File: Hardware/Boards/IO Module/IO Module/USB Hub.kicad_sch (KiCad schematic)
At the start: 0 parts

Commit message: Updated IO Module Schematics
Added Power, USB hub and USB-JTAG circuits
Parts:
- added C29: 10nF, Capacitor_SMD:C_0402_1005Metric, symbol Device:C_Small
- added C30, C32, C33, C34, C40, C41, C42, C43, C44, C45, C46, C47, C52, C53, C54, C55, C56, C57, C58, C59, C60, C61: 100nF, Capacitor_SMD:C_0402_1005Metric, symbol Device:C_Small
- added C31, C36, C48, C51: 1uF, Capacitor_SMD:C_0402_1005Metric, symbol Device:C_Small
- added C35, C37, C38, C39: 10uF, Capacitor_SMD:C_0603_1608Metric, symbol Device:C_Small
- added C49, C50: 18pF, Capacitor_SMD:C_0402_1005Metric, symbol Device:C_Small
- added D5: 1V1 FLT, LED_SMD:LED_0603_1608Metric, symbol Device:LED
- added Q2: IRLML6244, Package_TO_SOT_SMD:SOT-23, symbol Transistor_FET:IRLML6244
- added R32: 3.74K, Resistor_SMD:R_0402_1005Metric, symbol Device:R_US
- added R33, R38, R39, R40, R41: 10K, Resistor_SMD:R_0402_1005Metric, symbol Device:R_US
- added R34: 3.3K, Resistor_SMD:R_0402_1005Metric, symbol Device:R_US
- added R35: 1.13K, Resistor_SMD:R_0402_1005Metric, symbol Device:R_US
- added R36: 44.2K, Resistor_SMD:R_0402_1005Metric, symbol Device:R_US
- added R37: 1M, Resistor_SMD:R_0402_1005Metric, symbol Device:R_US
- added R42, R43, R45, R46, R47, R48, R49, R50, R51, R52: 33R, Resistor_SMD:R_0402_1005Metric, symbol Device:R_US
- added R44: 9.53K, Resistor_SMD:R_0402_1005Metric, symbol Device:R_US
- added U5: TUSB8041, Package_DFN_QFN:QFN-64-1EP_9x9mm_P0.5mm_EP6x6mm_ThermalVias, symbol Interface_USB:TUSB8041
- added U6: TPS74801AWDRC, Package_SON:VSON-10-1EP_3x3mm_P0.5mm_EP1.65x2.4mm_ThermalVias, symbol Regulator_Linear:TPS74801AWDRC
- added U7: TUSB542, IO_Module:TUSB542, symbol IO_Module:TUSB542
- added Y1: 24Mhz, Oscillator:Oscillator_SMD_Abracon_ASE-4Pin_3.2x2.5mm, symbol Device:Crystal_GND24_Small
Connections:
- new net: C48.1, U5.50 (GRSTz)
- new net: R44.1, U5.64 (USB_R1)
- new net: R40.1, R41.2, U7.10 (CFG_B2)
- new net: D5.1 (K), U6.3 (PG)
- new net: C29.1, U6.7 (SS)
- new net: D5.2 (A), R34.2
- new net: Q2.3 (D), R39.1, U7.16 (SEL)
- new net +1V1: C37.1, C38.1, C39.1, C40.1, C41.1, C42.1, C43.1, C44.1, C45.1, C46.1, C47.1, R32.2, U5.13 (VDD), U5.21 (VDD), U5.28 (VDD), U5.31 (VDD), U5.5 (VDD), U5.51 (VDD), U5.57 (VDD), U5.8 (VDD), U6.10 (OUT), U6.9 (OUT)
- new net +1V8: C35.1, C51.1, R39.2, R40.2, U6.1 (IN), U6.2 (IN), U6.5 (EN), U7.5 (VDD1V8)
- new net +3V3: C30.1, C31.1, C32.1, C33.1, C34.1, C36.1, R34.1, U5.16 (VDD33), U5.34 (VDD33), U5.52 (VDD33), U5.63 (VDD33), U6.4 (BIAS)
- new net GND: C29.2, C30.2, C31.2, C32.2, C33.2, C34.2, C35.2, C36.2, C37.2, C38.2, C39.2, C40.2, C41.2, C42.2, C43.2, C44.2, C45.2, C46.2, C47.2, C48.2, C49.2, C50.1, C51.2, Q2.2 (S), R33.1, R35.1, R38.1, R41.1, R44.2, U5.32 (PWRCTL4/BATEN4), U5.33 (PWRCTL3/BATEN3), U5.35 (PWRCTL2/BATEN2), U5.36 (PWRCTL1/BATEN1), U5.65 (VSS), U6.11 (GND), U6.6 (GND), U7.19 (EP), Y1.2, Y1.4
- new net HUB_XI: C50.2, R37.1, U5.62 (XI), Y1.3
- new net HUB_XO: C49.1, R37.2, U5.61 (XO), Y1.1
- new net PP1V1_FB: R32.1, R33.2, U6.8 (FB)
- new net PP_VUSB: R36.2
- new net RXA_N: C56.1, U7.17 (RX_AP_N)
- new net RXA_P: C57.1, U7.18 (RX_AP_P)
- new net SSTX1_N: C61.1, U5.4 (USB_SSTXM_DN1)
- new net SSTX1_P: C60.1, U5.3 (USB_SSTXP_DN1)
- new net TXA_N: C58.1, U7.14 (TX_AP_N)
- new net TXA_P: C59.1, U7.15 (TX_AP_P)
- new net TXC_1_N: C52.2, U7.7 (TX_CON_1_N)
- new net TXC_1_P: C53.2, U7.6 (TX_CON_1_P)
- new net TXC_2_N: C54.2, U7.11 (TX_CON_2_N)
- new net TXC_2_P: C55.2, U7.12 (TX_CON_2_P)
- new net USB1D_N: R46.2, U5.2 (USB_DM_DN1)
- new net USB1D_P: R45.2, U5.1 (USB_DP_DN1)
- new net USB2D_N: R48.2, U5.10 (USB_DM_DN2)
- new net USB2D_P: R47.2, U5.9 (USB_DP_DN2)
- new net USB2_D_N: R42.2
- new net USB2_D_P: R43.2
- new net USB2_RD_N: R42.1, U5.54 (USB_DM_UP)
- new net USB2_RD_P: R43.1, U5.53 (USB_DP_UP)
- new net USB3D_N: R50.2, U5.18 (USB_DM_DN3)
- new net USB3D_P: R49.2, U5.17 (USB_DP_DN3)
- new net USB3_RX1_N: U7.3 (RX_CON_1_N)
- new net USB3_RX1_P: U7.2 (RX_CON_1_P)
- new net USB3_RX2_N: U7.8 (RX_CON_2_N)
- new net USB3_RX2_P: U7.9 (RX_CON_2_P)
- new net USB3_RX_N: C56.2, U5.59 (USB_SSRXM_UP)
- new net USB3_RX_P: C57.2, U5.58 (USB_SSRXP_UP)
- new net USB3_TX1_N: C52.1
- new net USB3_TX1_P: C53.1
- new net USB3_TX2_N: C54.1
- new net USB3_TX2_P: C55.1
- new net USB3_TX_N: C58.2, U5.56 (USB_SSTXM_UP)
- new net USB3_TX_P: C59.2, U5.55 (USB_SSTXP_UP)
- new net USB4D_N: R52.2, U5.25 (USB_DM_DN4)
- new net USB4D_P: R51.2, U5.24 (USB_DP_DN4)
- new net USBPD_PLG_FLIP: Q2.1 (G), R38.2
- new net USB_FIFO_D_N: R46.1
- new net USB_FIFO_D_P: R45.1
- new net USB_FIFO_RX_N: U5.7 (USB_SSRXM_DN1)
- new net USB_FIFO_RX_P: U5.6 (USB_SSRXP_DN1)
- new net USB_FIFO_TX_N: C61.2
- new net USB_FIFO_TX_P: C60.2
- new net USB_JTAG_D_N: R48.1
- new net USB_JTAG_D_P: R47.1
- new net USB_MCU_D_N: R50.1
- new net USB_MCU_D_P: R49.1
- new net USB_SYSMON_D_N: R52.1
- new net USB_SYSMON_D_P: R51.1
- new net USB_VBUS_DET: R35.2, R36.1, U5.48 (USB_VBUS)
- no-connect marks 0 -> 27
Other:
- note added: "1V1 Core LDO"
- note added: "USB Conditioning + MUX"
- note added: "USB HUB"
- company: (none) -> Drexel University
- title: (none) -> USB Hub

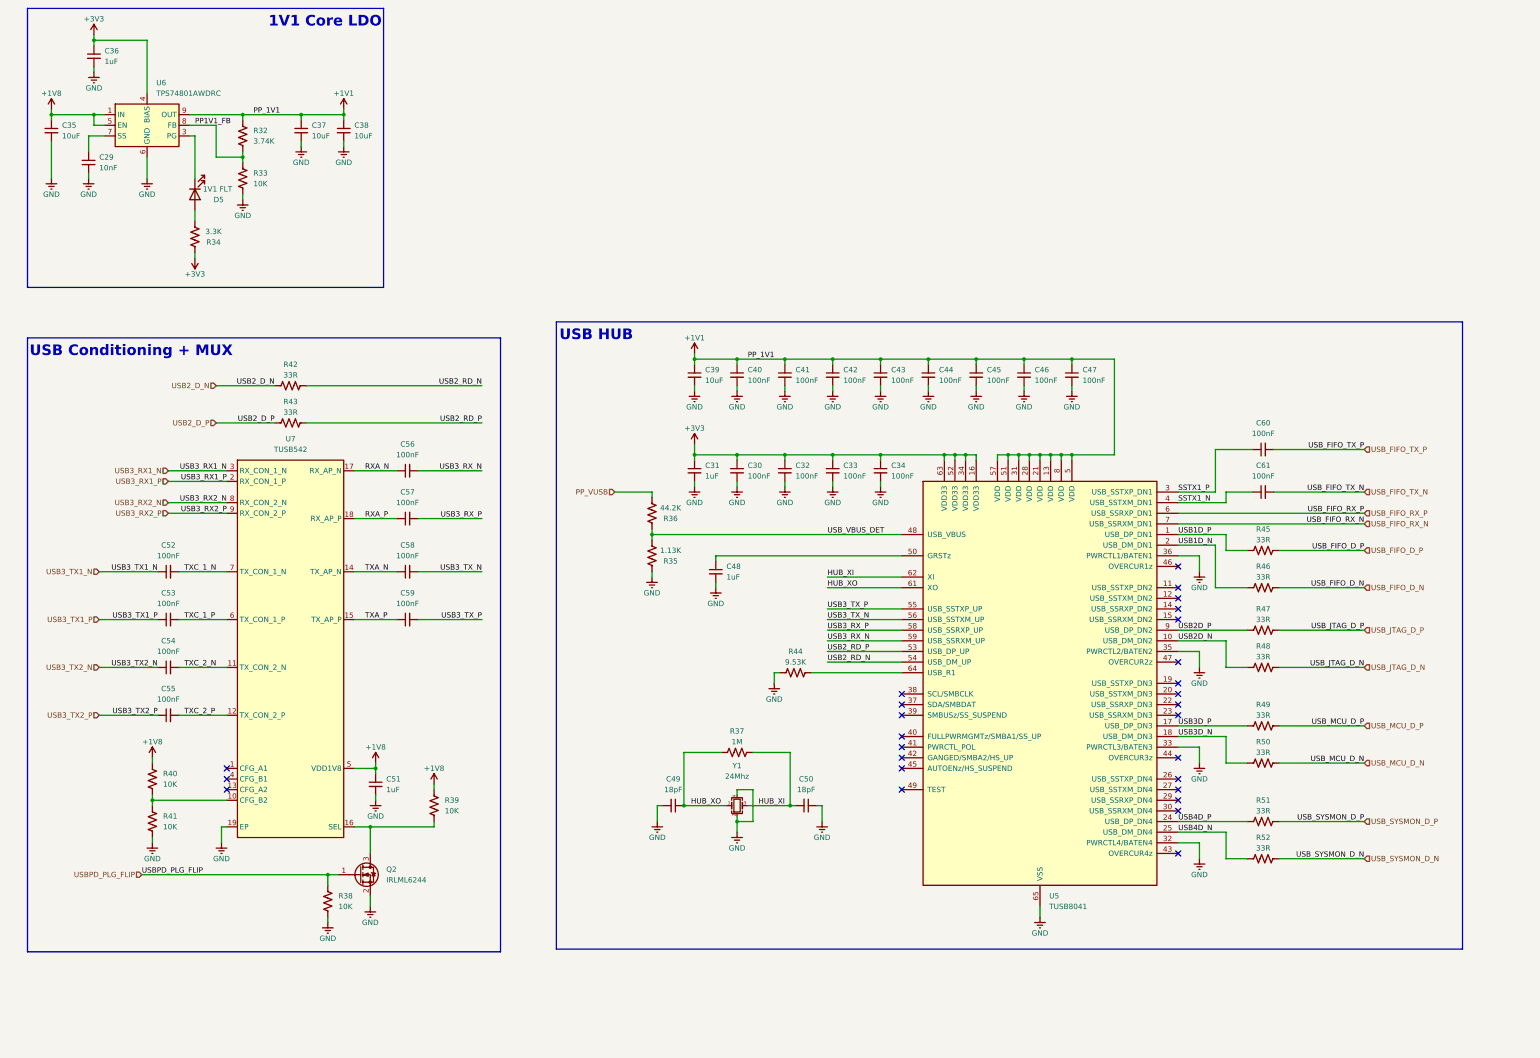
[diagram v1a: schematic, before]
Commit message: Completed IO Module Schematics
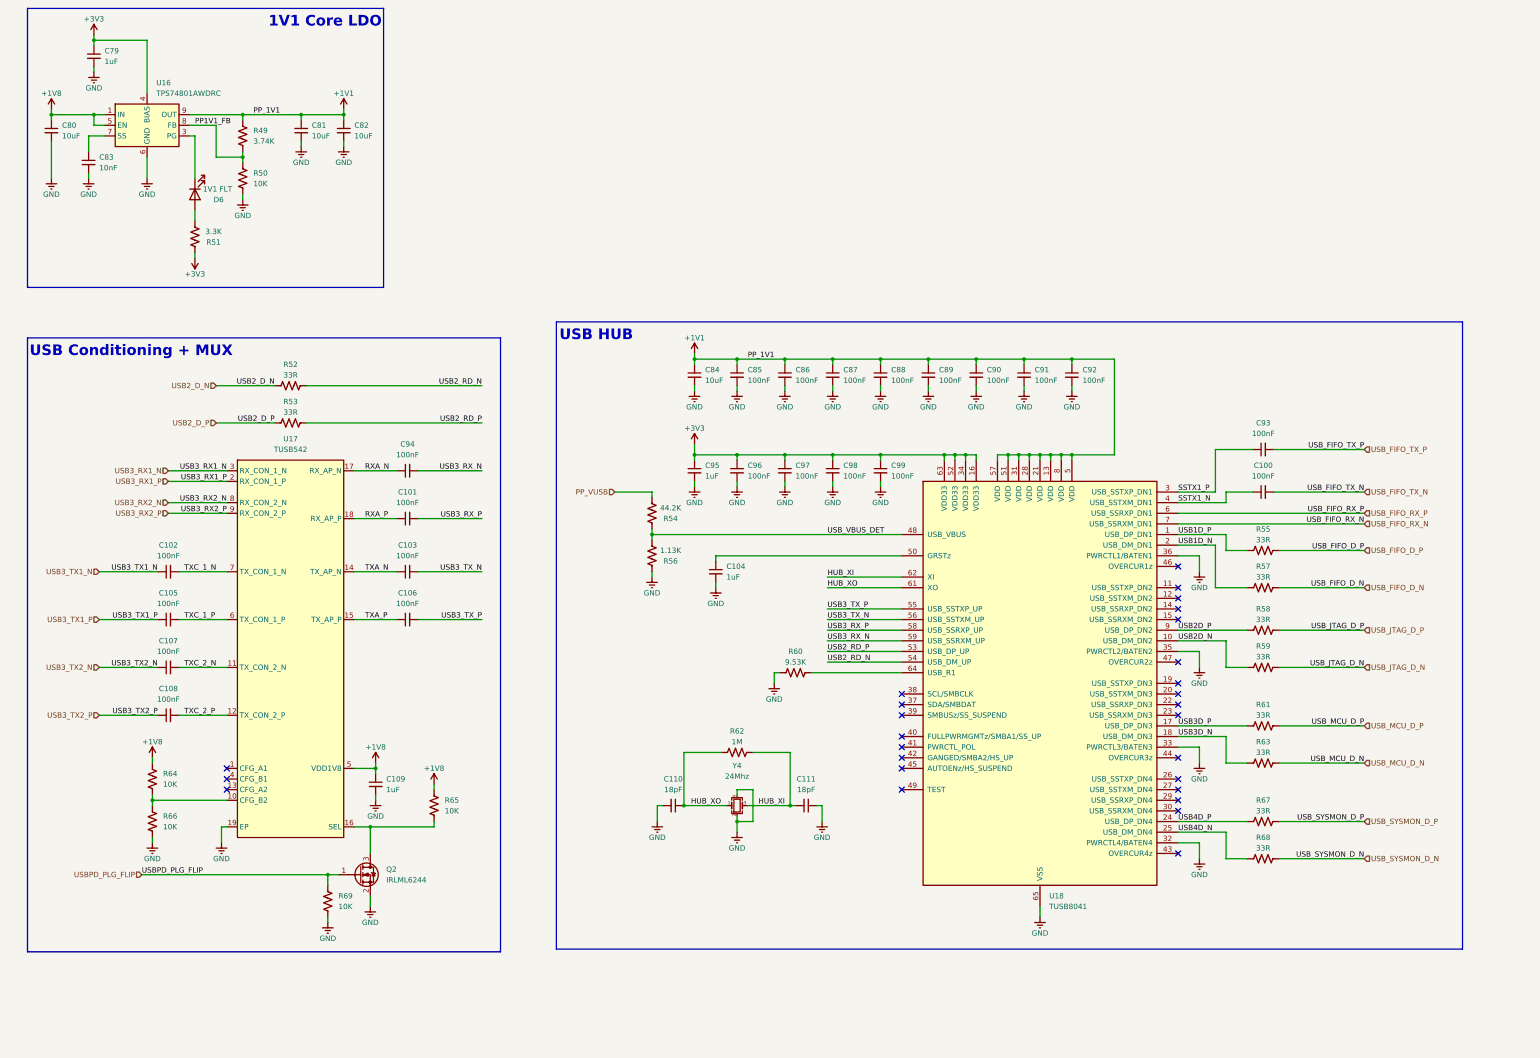
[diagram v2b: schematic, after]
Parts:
- renumbered C61 to C100, C57 to C101, C52 to C102, C58 to C103, C48 to C104, C53 to C105, C59 to C106, C54 to C107, C55 to C108, C51 to C109, C49 to C110, C50 to C111, C36 to C79, C35 to C80, C37 to C81, C38 to C82, C29 to C83, C39 to C84, C40 to C85, C41 to C86, C42 to C87, C43 to C88, C44 to C89, C45 to C90, C46 to C91, C47 to C92, C60 to C93, C56 to C94, C31 to C95, C30 to C96, C32 to C97, C33 to C98, C34 to C99, D5 to D6, R32 to R49, R33 to R50, R34 to R51, R42 to R52, R43 to R53, R36 to R54, R45 to R55, R35 to R56, R46 to R57, R47 to R58, R48 to R59, R44 to R60, R49 to R61, R37 to R62, R50 to R63, R40 to R64, R39 to R65, R41 to R66, R51 to R67, R52 to R68, R38 to R69, U6 to U16, U7 to U17, U5 to U18, Y1 to Y4

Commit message: Updated SCH with notes & annotations
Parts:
- removed Q2: IRLML6244, Package_TO_SOT_SMD:SOT-23, symbol Transistor_FET:IRLML6244
- removed U17: TUSB542, IO_Module:TUSB542, symbol IO_Module:TUSB542
- added C149, C150, C151, C152: 100nF, Capacitor_SMD:C_0402_1005Metric, symbol Device:C_Small
- added R104, R105, R106, R107, R108, R109, R110, R111, R112, R113, R114, R115, R116, R117: 1K, Resistor_SMD:R_0402_1005Metric, symbol Device:R_US
- added U24: TUSB1142, IO_Module:WQFN_142RNQT_TEX, symbol IO_Module:TUSB1142
- C101, C102, C103, C105, C106, C107, C108, C94: value 100nF -> 220nF
- C109: value 1uF -> 10uF; footprint Capacitor_SMD:C_0402_1005Metric -> Capacitor_SMD:C_0603_1608Metric
- R64, R69: value 10K -> 1K
- R65, R66: value 10K -> 1K; now not fitted
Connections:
- net +1V8: no longer C109.1, R64.2, R65.2
- net +3V3: now also C109.1, R65.2, R66.2, C149.1, C150.1, C151.1, C152.1, R110.2, R111.2, R112.2, R113.2, R114.2, R115.2, U24.1 (VCC), U24.20 (VCC), U24.28 (VCC), U24.6 (VCC)
- net GND: now also R64.1, C149.2, C150.2, C151.2, C152.2, R104.1, R105.1, R106.1, R107.1, R108.1, R109.1, R116.1, R117.1, U24.27 (TEST1), U24.41 (EPAD); no longer R66.1
- net RXA_N: now also U24.18 (SSRXn)
- net RXA_P: now also U24.19 (SSRXp)
- net TXA_N: now also U24.15 (SSTXn)
- net TXA_P: now also U24.16 (SSTXp)
- net TXC_1_N: now also U24.34 (CTX1n)
- net TXC_1_P: now also U24.33 (CTX1p)
- net TXC_2_N: now also U24.39 (CTX2n)
- net TXC_2_P: now also U24.40 (CTX2p)
- net USB3_RX1_N: now also U24.30 (CRX1p)
- net USB3_RX1_P: now also U24.31 (CRX1n)
- net USB3_RX2_N: now also U24.36 (CRX2n)
- net USB3_RX2_P: now also U24.37 (CRX2p)
- net USBPD_PLG_FLIP: now also U24.21 (FLIP/SCL); no longer R69.2
- net USB_HUB_RST: now reaches C104.1, U18.50 (GRSTz)
- net USB_HUB_REF: now reaches R60.1, U18.64 (USB_R1)
- net USSEQ1: now reaches R65.1
- net USSEQ1: now also R64.2, U24.2 (SSEQ1/A1)
- new net AEQCFG: R105.2, R111.1, U24.23 (AEQCFG)
- new net AEQENZ: R106.2, R112.1, U24.22 (AEQENZ/SDA)
- new net CEQ0: R108.2, R114.1, U24.38 (CEQ0)
- new net CEQ1: R109.2, R115.1, U24.29 (CEQ1)
- new net EQCFG: R104.2, R110.1, U24.3 (EQCFG)
- new net SLP_S0: R107.2, R113.1, U24.4 (SLP_S0)
- new net UMUX_MODE: R116.2, U24.17 (MODE)
- new net UMUX_VIO: R117.2, U24.14 (VIO_SEL)
- new net USBPD_PLG_EVNT: U24.26 (EN)
- new net USSEQ0: R66.1, R69.2, U24.35 (SSEQ0/A0)
- no-connect marks 27 -> 35
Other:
- moved on the sheet: C100, C101, C102, C103, C104, C105, C106, C107, C108, C110, C111, C84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

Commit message: Updated PCB routing for IO Module
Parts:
- C100, C101, C102, C103, C104, C105, C106, C107, C108, C110, C111, C149, C150, C151, C152, C79, C83, C85, C86, C87, C88, C89, C90, C91, C92, C93, C94, C95, C96, C97, C98, C99: footprint Capacitor_SMD:C_0402_1005Metric -> Capacitor_SMD:C_0201_0603Metric
- R104, R107, R111, R112, R114, R115, R65, R66: footprint Resistor_SMD:R_0402_1005Metric -> Resistor_SMD:R_0201_0603Metric; now fitted
- R105, R106, R108, R109, R110, R113, R116, R117, R49, R50, R51, R52, R53, R54, R55, R56, R57, R58, R59, R60, R61, R62, R63, R64, R67, R68, R69: footprint Resistor_SMD:R_0402_1005Metric -> Resistor_SMD:R_0201_0603Metric

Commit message: Completed IO Module PCB Layout
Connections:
- net USB_JTAG_D_N: now also R63.1; no longer R59.1
- net USB_JTAG_D_P: now also R61.1; no longer R58.1
- net USB_MCU_D_N: now also R68.1; no longer R63.1
- net USB_MCU_D_P: now also R67.1; no longer R61.1
- net USB_SYSMON_D_N: now also R59.1; no longer R68.1
- net USB_SYSMON_D_P: now also R58.1; no longer R67.1

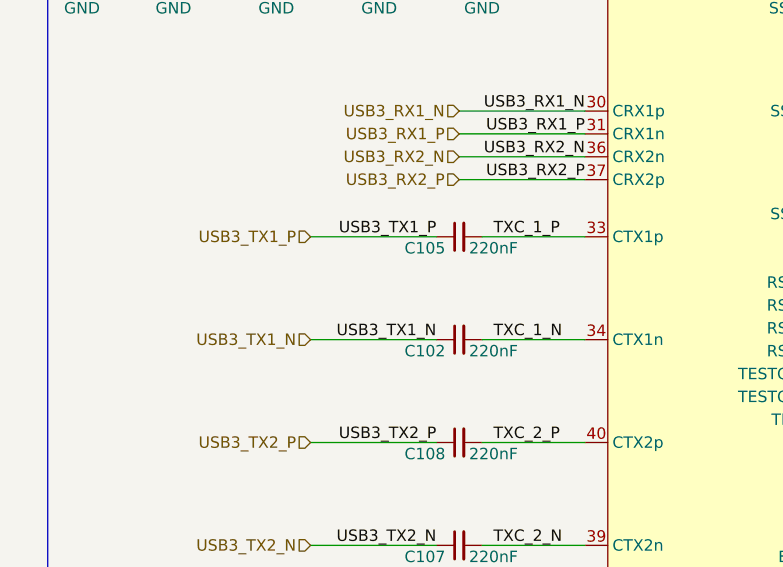
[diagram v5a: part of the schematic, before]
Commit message: Cleaned up routing for IO module
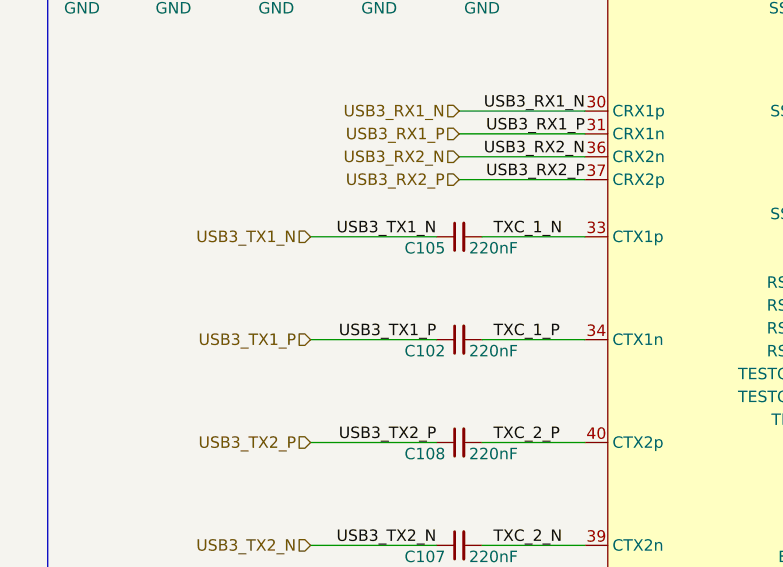
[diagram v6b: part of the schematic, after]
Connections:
- net TXC_1_N: now also C105.2, U24.33 (CTX1p); no longer C102.2, U24.34 (CTX1n)
- net TXC_1_P: now also C102.2, U24.34 (CTX1n); no longer C105.2, U24.33 (CTX1p)
- net USB3_TX1_N: now also C105.1; no longer C102.1
- net USB3_TX1_P: now also C102.1; no longer C105.1
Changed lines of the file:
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@@
+		)
+	)
+	(label "USB3_TX1_P"
+		(at 72.39 173.99 180)
+		(fields_autoplaced yes)
+		(effects
+			(font
+				(size 1.27 1.27)
+			)
+			(justify right bottom)
 		)
 	)
@@
 		)
 	)
-	(label "USB3_TX1_N"
-		(at 72.39 173.99 180)
-		(fields_autoplaced yes)
-		(effects
-			(font
-				(size 1.27 1.27)
-			)
-			(justify right bottom)
+	(label "TXC_1_N"
+		(at 78.74 162.56 0)
+		(fields_autoplaced yes)
+		(effects
+			(font
+				(size 1.27 1.27)
+			)
+			(justify left bottom)
 		)
 	)
@@
 		)
 	)
-	(label "TXC_1_P"
-		(at 78.74 162.56 0)
-		(fields_autoplaced yes)
-		(effects
-			(font
-				(size 1.27 1.27)
-			)
-			(justify left bottom)
-		)
-	)
 	(label "USB4D_N"
 		(at 321.31 214.63 0)
@@
 		)
 	)
+	(label "TXC_1_P"
+		(at 78.74 173.99 0)
+		(fields_autoplaced yes)
+		(effects
+			(font
+				(size 1.27 1.27)
+			)
+			(justify left bottom)
+		)
+	)
 	(label "USB3D_P"
 		(at 321.31 189.23 0)
@@
 		)
 	)
-	(label "TXC_1_N"
-		(at 78.74 173.99 0)
-		(fields_autoplaced yes)
-		(effects
-			(font
-				(size 1.27 1.27)
-			)
-			(justify left bottom)
-		)
-	)
 	(label "USB_VBUS_DET"
 		(at 237.49 143.51 0)
@@
 		)
 	)
+	(label "USB3_TX1_N"
+		(at 72.39 162.56 180)
+		(fields_autoplaced yes)
+		(effects
+			(font
+				(size 1.27 1.27)
+			)
+			(justify right bottom)
+		)
+	)
 	(label "USB3_TX_P"
 		(at 237.49 161.29 0)
@@
 		)
 	)
-	(label "USB3_TX1_P"
-		(at 72.39 162.56 180)
-		(fields_autoplaced yes)
-		(effects
-			(font
-				(size 1.27 1.27)
-			)
-			(justify right bottom)
-		)
-	)
 	(label "SSTX1_N"
 		(at 321.31 135.89 0)
@@
 		)
 	)
+	(hierarchical_label "USB3_TX1_P"
+		(shape input)
+		(at 58.42 173.99 180)
+		(fields_autoplaced yes)
+		(effects
+			(font
+				(size 1.27 1.27)
+			)
+			(justify right)
+		)
+	)
 	(hierarchical_label "USB_MCU_D_P"
 		(shape input)
@@
 		)
 	)
-	(hierarchical_label "USB3_TX1_P"
+	(hierarchical_label "USB_JTAG_D_P"
+		(shape input)
+		(at 365.76 189.23 0)
+		(fields_autoplaced yes)
+		(effects
+			(font
+				(size 1.27 1.27)
+			)
+			(justify left)
+		)
+	)
+	(hierarchical_label "USB2_D_N"
+		(shape input)
+		(at 85.09 104.14 180)
+		(fields_autoplaced yes)
+		(effects
+			(font
+				(size 1.27 1.27)
+			)
+			(justify right)
+		)
+	)
+	(hierarchical_label "USB_FIFO_RX_P"
+		(shape input)
+		(at 365.76 138.43 0)
+		(fields_autoplaced yes)
+		(effects
+			(font
+				(size 1.27 1.27)
+			)
+			(justify left)
+		)
+	)
+	(hierarchical_label "USB3_RX2_N"
+		(shape input)
+		(at 74.93 153.67 180)
+		(fields_autoplaced yes)
+		(effects
+			(font
+				(size 1.27 1.27)
+			)
+			(justify right)
+		)
+	)
+	(hierarchical_label "USB3_TX1_N"
 		(shape input)
 		(at 58.42 162.56 180)
 		(fields_autoplaced yes)
 		(effects
-			(font
-				(size 1.27 1.27)
-			)
-			(justify right)
-		)
-	)
-	(hierarchical_label "USB_JTAG_D_P"
-		(shape input)
-		(at 365.76 189.23 0)
-		(fields_autoplaced yes)
-		(effects
-			(font
-				(size 1.27 1.27)
-			)
-			(justify left)
-		)
-	)
-	(hierarchical_label "USB3_TX1_N"
-		(shape input)
-		(at 58.42 173.99 180)
-		(fields_autoplaced yes)
-		(effects
-			(font
-				(size 1.27 1.27)
-			)
-			(justify right)
-		)
-	)
-	(hierarchical_label "USB2_D_N"
-		(shape input)
-		(at 85.09 104.14 180)
-		(fields_autoplaced yes)
-		(effects
-			(font
-				(size 1.27 1.27)
-			)
-			(justify right)
-		)
-	)
-	(hierarchical_label "USB_FIFO_RX_P"
-		(shape input)
-		(at 365.76 138.43 0)
-		(fields_autoplaced yes)
-		(effects
-			(font
-				(size 1.27 1.27)
-			)
-			(justify left)
-		)
-	)
-	(hierarchical_label "USB3_RX2_N"
-		(shape input)
-		(at 74.93 153.67 180)
-		(fields_autoplaced yes)
-		(effects
